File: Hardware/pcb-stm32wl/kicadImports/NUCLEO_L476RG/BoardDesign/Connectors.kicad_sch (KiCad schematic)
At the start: 29 parts, among them CN10 Header 10X1_Female, CN11 Header 8X1_Female, CN12 Header 19X2, CN7 Header 19X2, CN8 Header 8X1_Female, CN9 Header 6X1_Female

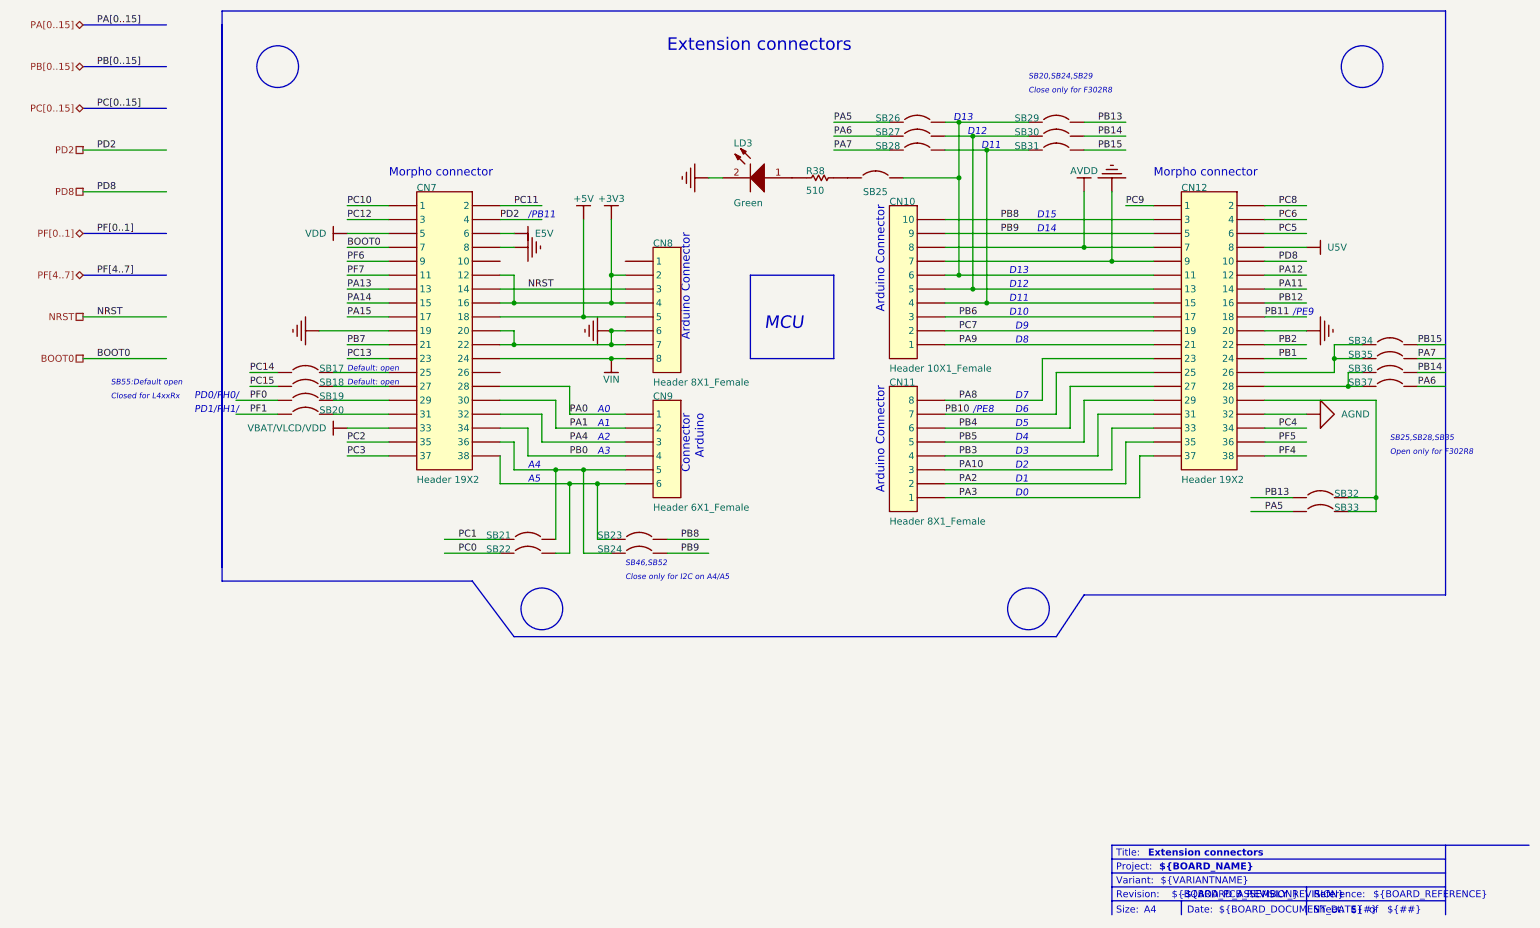
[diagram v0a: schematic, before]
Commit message: . Re-imported NUCLEO_L476RG/BoardDesign/* files using KiCad 9.0.0 one at a time (to avoid a bug evident in misconnections in MCU_64), copied the schematic contents into local kicad_sch files with the same names, prefixed with NUCLEO_L476RG_*
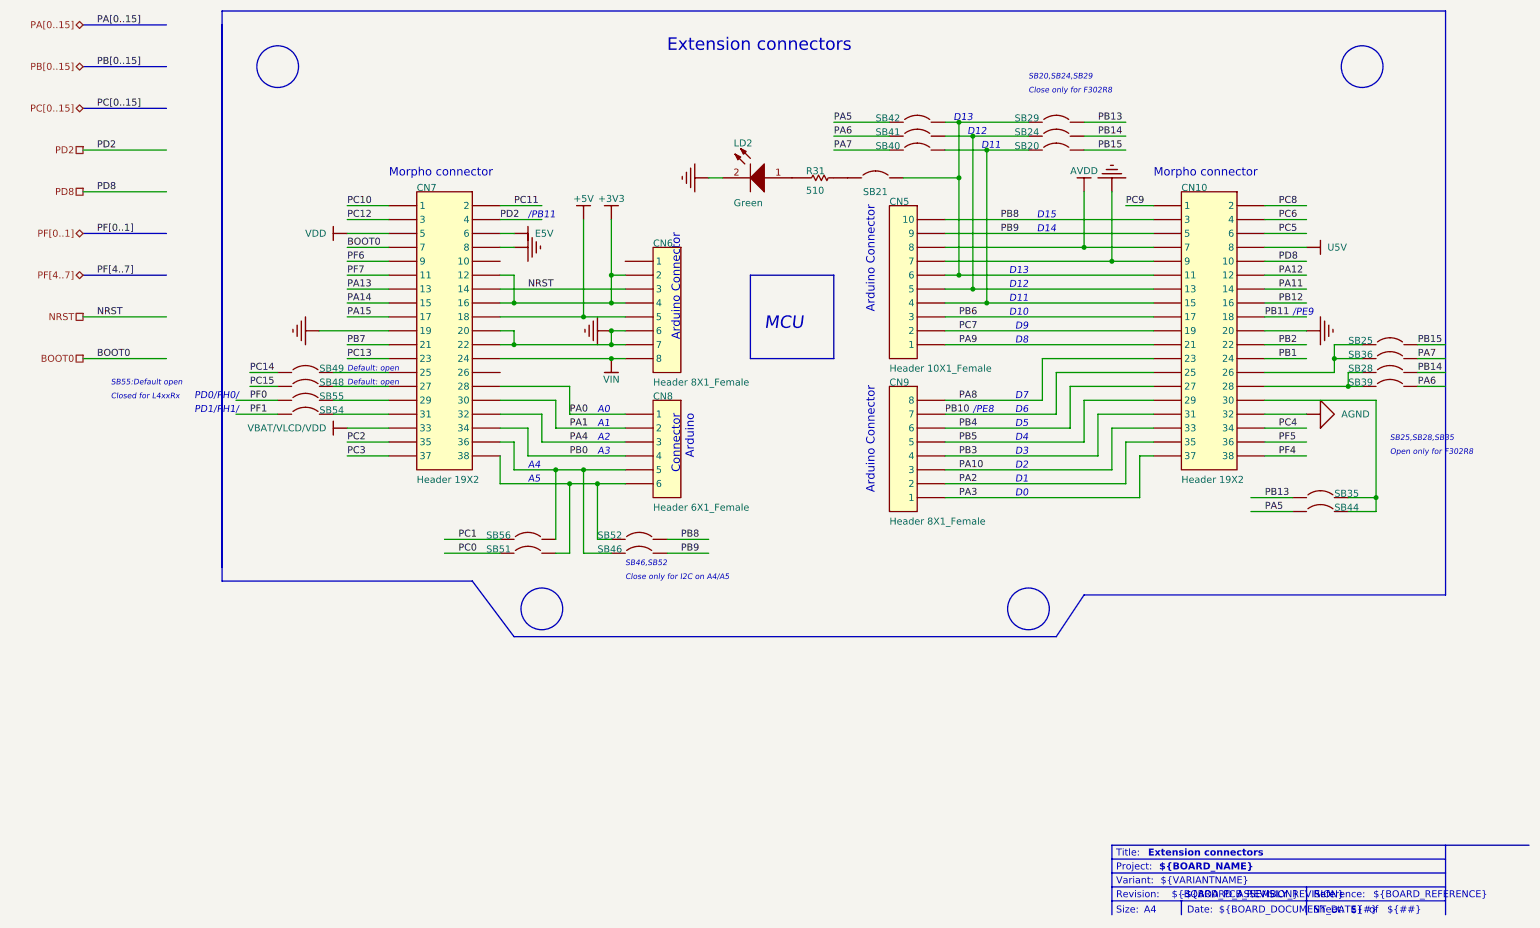
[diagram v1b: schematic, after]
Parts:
- removed CN10: Header 10X1_Female, 1*10P_FEMALE, symbol Project_Overview-altium-import:U_Connectors_2_Header 10X1_Female
- removed CN11: Header 8X1_Female, 1*8P_FEMALE, symbol Project_Overview-altium-import:U_Connectors_2_Header 8X1_Female
- removed CN12, CN7: Header 19X2, 2*19P, symbol Project_Overview-altium-import:U_Connectors_0_Header 19X2
- removed CN8: Header 8X1_Female, 1*8P_FEMALE, symbol Project_Overview-altium-import:U_Connectors_0_Header 8X1_Female
- removed CN9: Header 6X1_Female, 1*6P_FEMALE, symbol Project_Overview-altium-import:U_Connectors_0_Header 6X1_Female
- removed LD3: Green, 0603D, symbol Project_Overview-altium-import:U_Connectors_0_mirrored_LED2
- removed R38: 510, 0603R, symbol Project_Overview-altium-import:U_Connectors_2_Res1_0
- removed SB17, SB18, SB19, SB20, SB32, SB33, SB34, SB35, SB36, SB37: Circuit Breaker, JP2_SMD, symbol Project_Overview-altium-import:U_Connectors_0_mirrored_Circuit Breaker
- removed SB21, SB22, SB23, SB24, SB25, SB26, SB27, SB28, SB29, SB30, SB31: Circuit Breaker, JP2_SMD, symbol Project_Overview-altium-import:U_Connectors_0_Circuit Breaker
- added CN10, CN7: Header 19X2, 2*19P, symbol Connectors-altium-import:root_0_Header 19X2_Nucleo_64_1.SCHLIB
- added CN5: Header 10X1_Female, 1*10P_FEMALE, symbol Connectors-altium-import:root_2_Header 10X1_Female_Nucleo_64.SCHLIB
- added CN6: Header 8X1_Female, 1*8P_FEMALE, symbol Connectors-altium-import:root_0_Header 8X1_Female_Nucleo_64.SCHLIB
- added CN8: Header 6X1_Female, 1*6P_FEMALE, symbol Connectors-altium-import:root_0_Header 6X1_Female_Nucleo_64.SCHLIB
- added CN9: Header 8X1_Female, 1*8P_FEMALE, symbol Connectors-altium-import:root_2_Header 8X1_Female_Nucleo_64.SCHLIB
- added LD2: Green, 0603D, symbol Connectors-altium-import:root_0_mirrored_LED2_Miscellaneous Devices.IntLib
- added R31: 510, 0603R, symbol Connectors-altium-import:root_2_Res1_Miscellaneous Devices.IntLib_0
- added SB20, SB21, SB24, SB29, SB40, SB41, SB42, SB46, SB51, SB52, SB56: Circuit Breaker, JP2_SMD, symbol Connectors-altium-import:root_0_Circuit Breaker_MCD_TOOLS.SCHLIB
- added SB25, SB28, SB35, SB36, SB39, SB44, SB48, SB49, SB54, SB55: Circuit Breaker, JP2_SMD, symbol Connectors-altium-import:root_0_mirrored_Circuit Breaker_MCD_TOOLS.SCHLIB
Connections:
- net +3V3: now also CN6.2, CN6.4, CN7.12, CN7.16
- net +5V: now also CN6.5, CN7.18
- net AGND: now also CN10.32
- net AVDD: now also CN10.7, CN5.8
- net BOOT0: now also CN7.7
- net E5V: now also CN7.6
- net GND: now also CN10.20, CN10.9, CN5.7, CN6.6, CN6.7, CN7.19, CN7.20, CN7.22, CN7.8, LD2.2 (K)
- net NRST: now also CN6.3, CN7.14
- net PA0: now also CN7.28, CN8.1
- net PA1: now also CN7.30, CN8.2
- net PA10: now also CN10.33, CN9.3
- net PA11: now also CN10.14
- net PA12: now also CN10.12
- net PA13: now also CN7.13
- net PA14: now also CN7.15
- net PA15: now also CN7.17
- net PA2: now also CN10.35, CN9.2
- net PA3: now also CN10.37, CN9.1
- net PA4: now also CN7.32, CN8.3
- net PA5: now also SB42.1, SB44.2
- net PA6: now also SB39.1, SB41.1
- net PA7: now also SB36.1, SB40.1
- net PA8: now also CN10.23, CN9.8
- net PA9: now also CN10.21, CN5.1
- net PB0: now also CN7.34, CN8.4
- net PB1: now also CN10.24
- net PB10: now also CN10.25, CN9.7
- net PB11: now also CN10.18
- net PB12: now also CN10.16
- net PB13: now also SB29.2, SB35.2
- net PB14: now also SB24.2, SB28.1
- net PB15: now also SB20.2, SB25.1
- net PB2: now also CN10.22
- net PB3: now also CN10.31, CN9.4
- net PB4: now also CN10.27, CN9.6
- net PB5: now also CN10.29, CN9.5
- net PB6: now also CN10.17, CN5.3
- net PB7: now also CN7.21
- net PB8: now also CN10.3, CN5.10, SB52.2
- net PB9: now also CN10.5, CN5.9, SB46.2
- net PC0: now also SB51.1
- net PC1: now also SB56.1
- net PC10: now also CN7.1
- net PC11: now also CN7.2
- net PC12: now also CN7.3
- net PC13: now also CN7.23
- net PC14: now also SB49.2
- net PC15: now also SB48.2
- net PC2: now also CN7.35
- net PC3: now also CN7.37
- net PC4: now also CN10.34
- net PC5: now also CN10.6
- net PC6: now also CN10.4
- net PC7: now also CN10.19, CN5.2
- net PC8: now also CN10.2
- net PC9: now also CN10.1
- net PD2: now also CN7.4
- net PD8: now also CN10.10
- net PF0: now also SB55.2
- net PF1: now also SB54.2
- net PF4: now also CN10.38
- net PF5: now also CN10.36
- net PF6: now also CN7.9
- net PF7: now also CN7.11
- net U5V: now also CN10.8
- net VBAT/VLCD/VDD: now also CN7.33
- net VDD: now also CN7.5
- net VIN: now also CN6.8, CN7.24
- new net: CN10.30, SB35.1, SB44.1
- new net: CN7.36, CN8.5, SB46.1, SB56.2
- new net: R31.1, SB21.1
- new net: CN10.11, CN5.6, SB21.2, SB29.1, SB42.2
- new net: CN10.28, SB28.2, SB39.2
- new net: CN7.38, CN8.6, SB51.2, SB52.1
- new net: CN7.27, SB48.1
- new net: CN7.25, SB49.1
- new net: CN10.13, CN5.5, SB24.1, SB41.2
- new net: CN10.15, CN5.4, SB20.1, SB40.2
- new net: CN10.26, SB25.2, SB36.2
- new net: CN7.29, SB55.1
- new net: CN7.31, SB54.1
- new net: LD2.1 (A), R31.2
